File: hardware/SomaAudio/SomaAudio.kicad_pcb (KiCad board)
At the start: 2 copper layers, 74 x 78.8 mm, 14 parts, among them CN1 0.1uF, CN2 0.1uF, IC1 DG406DJ, J17 I2C, J2 Audio GND +, J3 Audio Out, J4 VIN, J5 Audio IN 1, J6 Audio IN 2, U1 MCP23017_SP

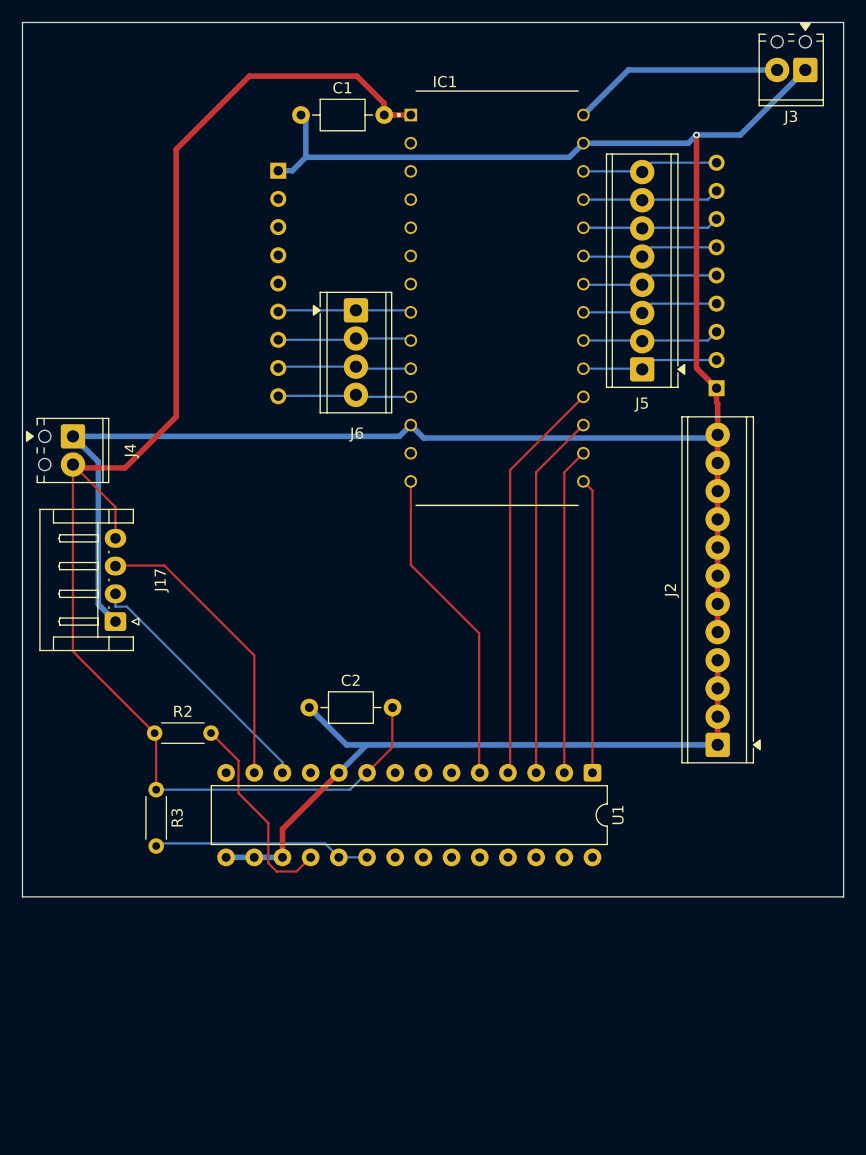
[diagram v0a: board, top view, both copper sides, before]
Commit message: hardware: combo board, LED board, production outputs, arduino firmware
Co-Authored-By: Claude Opus 5.5 (1M context) <noreply@anthropic.com>
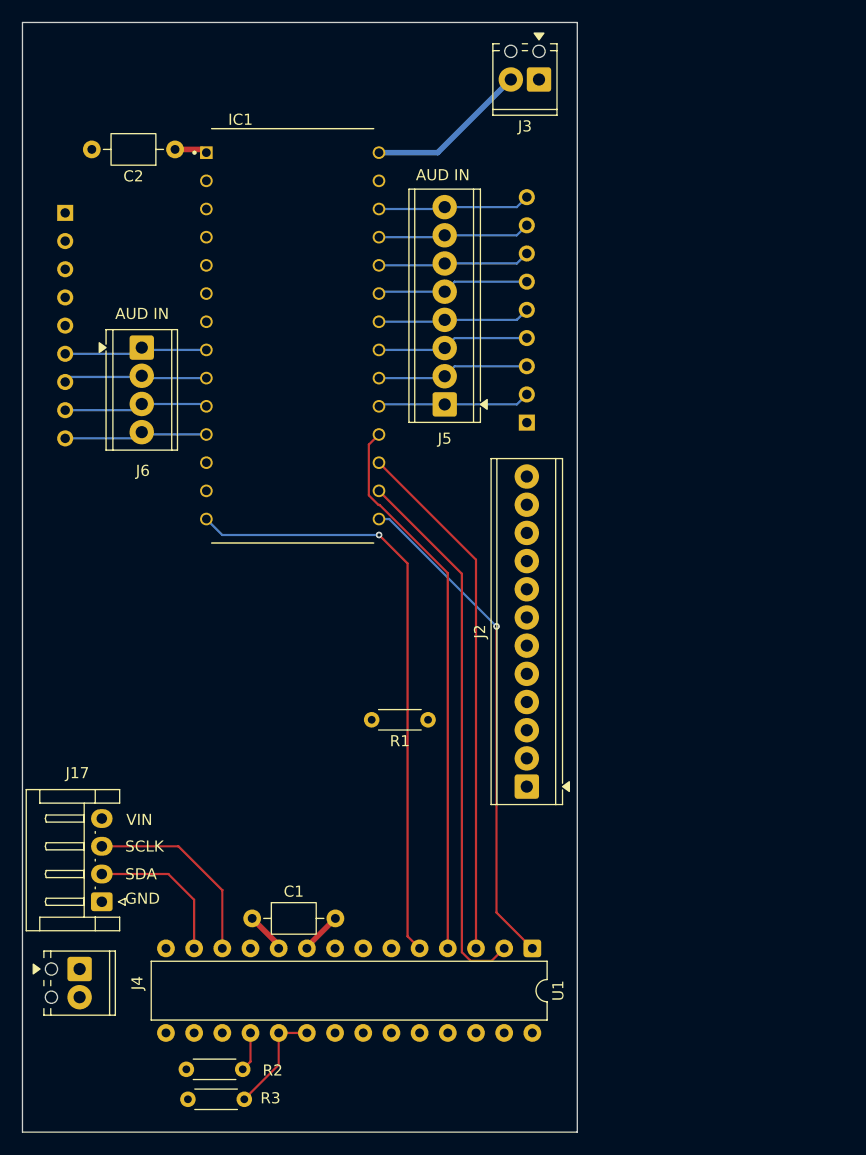
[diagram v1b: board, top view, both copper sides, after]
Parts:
- added R1: 0 OHM, Resistor_THT:R_Axial_DIN0204_L3.6mm_D1.6mm_P5.08mm_Horizontal, F.Cu at (137.5, 113.1)
- moved C1 72.5 mm to (121.7, 131.0)
- moved C2 51.7 mm to (114.7, 61.7), turned to 180 degrees
- moved J4 48.0 mm to (106.1, 135.6)
- moved R2 30.4 mm to (115.7, 144.6)
- moved R3 28.0 mm to (115.9, 147.3), turned to 0 degrees
- moved J17 25.3 mm to (108.1, 129.5)
- moved J3 24.0 mm to (147.5, 55.4)
- moved J6 19.6 mm to (111.7, 79.6)
- moved CN2 19.6 mm to (104.8, 67.4)
- moved IC1 18.7 mm to (125.3, 78.5)
- moved J5 18.1 mm to (139.0, 84.7)
- moved J2 17.6 mm to (146.4, 119.1)
- moved CN1 17.4 mm to (146.4, 86.3)
- moved U1 16.7 mm to (146.9, 133.7)
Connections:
- C2 pad 1: GND -> VCC 5V
- C2 pad 2: VCC 5V -> GNDA
- CN1 pad 1: GND -> GNDA
- CN2 pad 1: GND -> GNDA
- IC1 pad 12: GND -> GNDA
- IC1 pad 27: GND -> GNDA
- J2 pad 1: GND -> GNDA
- J2 pad 10: GND -> GNDA
- J2 pad 11: GND -> GNDA
- J2 pad 12: GND -> GNDA
- J2 pad 2: GND -> GNDA
- J2 pad 3: GND -> GNDA
- J2 pad 4: GND -> GNDA
- J2 pad 5: GND -> GNDA
- J2 pad 6: GND -> GNDA
- J2 pad 7: GND -> GNDA
- J2 pad 8: GND -> GNDA
- J2 pad 9: GND -> GNDA
- J3 pad 1: GND -> GNDA
- U1 pad 12: Net-(J17-Pin_2) -> Net-(J17-Pin_3)
- U1 pad 13: Net-(J17-Pin_3) -> Net-(J17-Pin_2)
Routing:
- net GND: track 242.4 -> 3.38 mm, vias 1 -> 0
- net VCC 5V: track 128.5 -> 6.17 mm
- net Net-(IC1-A3): track 28.8 -> 54.9 mm, vias 0 -> 1
- net Net-(IC1-A1): track 29.5 -> 49.3 mm
- net Net-(IC1-A2): track 26.6 -> 45.0 mm, vias 0 -> 1
- net Net-(U1-~{RESET}): track 18.5 -> 3.57 mm
- net Net-(IC1-A0): track 33.1 -> 47.4 mm
- net Net-(IC1-EN): track 36.7 -> 49.7 mm
- net Net-(U1-INTA): track 19.6 -> 9.80 mm
- net Net-(J17-Pin_2): track 23.0 -> 13.7 mm
- net Net-(J17-Pin_3): track 26.5 -> 17.8 mm
- net Net-(IC1-D): track 19.1 -> 14.6 mm
- net /S4: track 12.4 -> 13.5 mm
- net /S3: track 12.4 -> 13.5 mm
- net /S1: track 12.4 -> 13.5 mm
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- added copper zone on In1.Cu, net GND
- added copper zone on In1.Cu, net GNDA
- added copper zone on In2.Cu, net VCC 5V
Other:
- board size 74 x 78.8 mm -> 50 x 100 mm
- copper layers 2 -> 4
- board text added: "AUD IN"
- board text added: "GND"
- board text added: "SCLK"
- board text added: "SDA"
- board text added: "SOMA AUDIO - rev 0.1 graykai.art"
- board text added: "VIN"
